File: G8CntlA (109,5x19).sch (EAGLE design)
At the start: 24 parts, among them SW1 TL2201

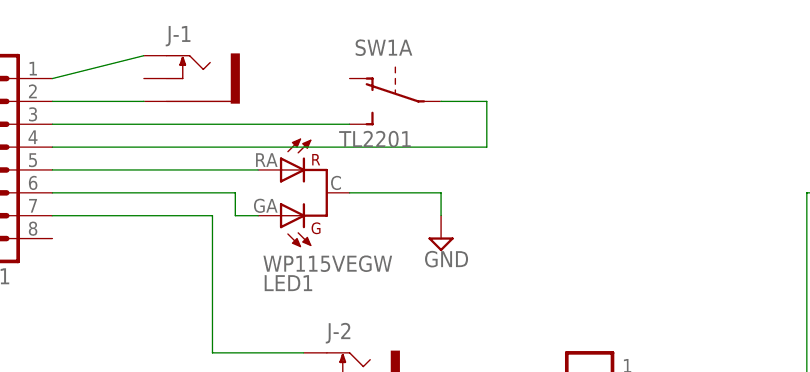
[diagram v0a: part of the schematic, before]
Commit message: Add files via upload
replaced switch
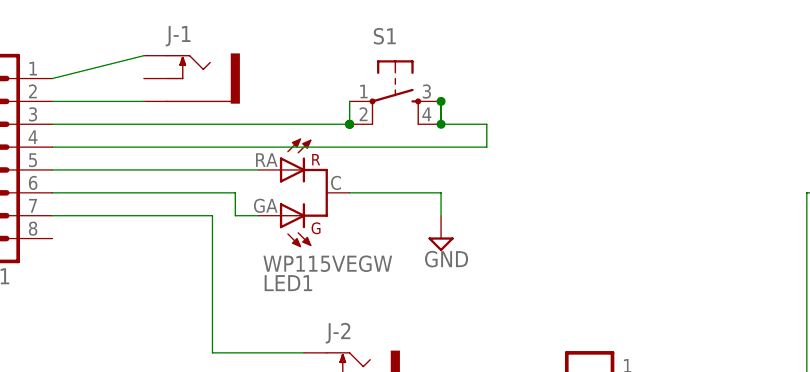
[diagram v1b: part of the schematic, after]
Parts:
- removed SW1: TL2201, tr-switch:TL2201
- added S1: (no value), !tactile-pth:SPARKFUN_TAC_SWITCHPTH
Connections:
- net N$1: now also S1.1, S1.2; no longer SW1A.NO
- net N$2: now also S1.3, S1.4; no longer SW1A.C
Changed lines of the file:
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@@
 <?xml version="1.0" encoding="utf-8"?>
 <!DOCTYPE eagle SYSTEM "eagle.dtd">
-<eagle version="6.4">
+<eagle version="9.1.1">
 <drawing>
 <settings>
 <setting alwaysvectorfont="no"/>
+<setting keepoldvectorfont="yes"/>
 <setting verticaltext="up"/>
 </settings>
@@
 <layer number="56" name="wert" color="7" fill="1" visible="no" active="no"/>
 <layer number="57" name="tCAD" color="7" fill="1" visible="no" active="no"/>
+<layer number="88" name="SimResults" color="9" fill="1" visible="yes" active="yes"/>
+<layer number="89" name="SimProbes" color="9" fill="1" visible="yes" active="yes"/>
 <layer number="90" name="Modules" color="7" fill="1" visible="yes" active="yes"/>
 <layer number="91" name="Nets" color="2" fill="1" visible="yes" active="yes"/>
@@
 <part name="LED7" library="tr-led" deviceset="WP115VEGW" device=""/>
 <part name="LED8" library="tr-led" deviceset="WP115VEGW" device=""/>
-<part name="SW1" library="tr-switch" deviceset="TL2201" device=""/>
 <part name="SUPPLY1" library="supply2" deviceset="GND" device=""/>
 <part name="SUPPLY2" library="supply2" deviceset="GND" device=""/>
@@
 <part name="J-1" library="!MusicThingModular" deviceset="THONKICONN" device="NEW"/>
 <part name="J-2" library="!MusicThingModular" deviceset="THONKICONN" device="NEW"/>
+<part name="S1" library="!tactile-pth" deviceset="SPARKFUN_TAC_SWITCH" device="PTH"/>
 </parts>
 <sheets>
@@
 <attribute name="VALUE" x="234.188" y="145.415" size="1.778" layer="96" rot="MR180"/>
 </instance>
-<instance part="SW1" gate="A" x="68.58" y="200.66" rot="MR270"/>
 <instance part="SUPPLY1" gate="GND" x="73.66" y="185.42"/>
 <instance part="SUPPLY2" gate="GND" x="55.88" y="165.1"/>
@@
 <instance part="J-1" gate="G$1" x="45.72" y="203.2"/>
 <instance part="J-2" gate="G$1" x="63.5" y="170.18"/>
+<instance part="S1" gate="S" x="68.58" y="200.66"/>
 </instances>
 <busses>
@@
 <wire x1="30.48" y1="198.12" x2="63.5" y2="198.12" width="0.1524" layer="91"/>
 <pinref part="SV1" gate="1" pin="3"/>
-<pinref part="SW1" gate="A" pin="NO"/>
+<pinref part="S1" gate="S" pin="2"/>
+<junction x="63.5" y="198.12"/>
+<pinref part="S1" gate="S" pin="1"/>
+<wire x1="63.5" y1="198.12" x2="63.5" y2="200.66" width="0.1524" layer="91"/>
+<junction x="63.5" y="198.12"/>
 </segment>
 </net>
 <net name="N$2" class="0">
 <segment>
-<pinref part="SW1" gate="A" pin="C"/>
-<wire x1="73.66" y1="200.66" x2="78.74" y2="200.66" width="0.1524" layer="91"/>
+<wire x1="73.66" y1="198.12" x2="78.74" y2="198.12" width="0.1524" layer="91"/>
 <wire x1="30.48" y1="195.58" x2="78.74" y2="195.58" width="0.1524" layer="91"/>
-<wire x1="78.74" y1="195.58" x2="78.74" y2="200.66" width="0.1524" layer="91"/>
+<wire x1="78.74" y1="195.58" x2="78.74" y2="198.12" width="0.1524" layer="91"/>
 <pinref part="SV1" gate="1" pin="4"/>
+<pinref part="S1" gate="S" pin="4"/>
+<junction x="73.66" y="198.12"/>
+<pinref part="S1" gate="S" pin="3"/>
+<wire x1="73.66" y1="198.12" x2="73.66" y2="200.66" width="0.1524" layer="91"/>
+<wire x1="73.66" y1="198.12" x2="73.66" y2="200.66" width="0.1524" layer="91"/>
+<junction x="73.66" y="200.66"/>
+<wire x1="73.66" y1="200.66" x2="73.66" y2="198.12" width="0.1524" layer="91"/>
 </segment>
 </net>
